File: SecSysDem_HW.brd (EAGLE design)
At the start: 99 x 80 mm, 47 parts, among them Q1 2N3904, T1 MOSFET_NCHANNEL_ENHANCEMENT2N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, T2 MOSFET_NCHANNEL_ENHANCEMENT2N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, T3 MOSFET_NCHANNEL_ENHANCEMENT2N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, U1 XPLAINED_MINI_PINOUT, U2 PCF8574_IO_EXPANDER, U4 FT24C512A, U5 MCP4901-E/SN, X1 C-GRID-06-70553, X5 C-GRID-02-70543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

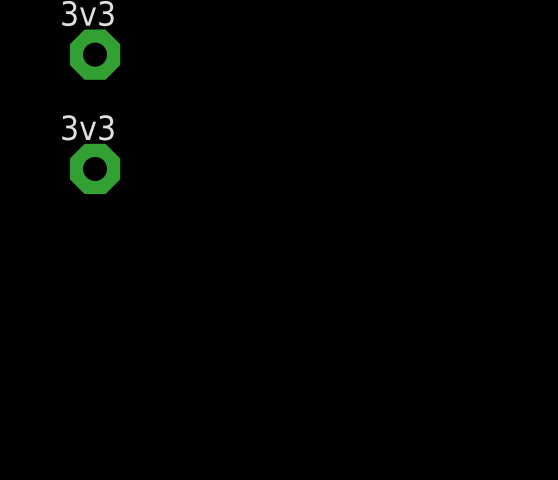
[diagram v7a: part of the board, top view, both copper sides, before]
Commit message: Switched IO expander pins to be keypad pins.
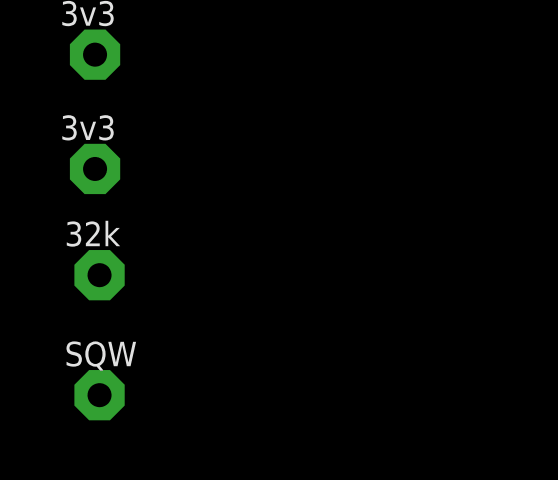
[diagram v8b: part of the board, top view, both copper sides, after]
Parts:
- added V10: SQW, Luke:VIA1
- added V2: 32k, Luke:VIA1
- IC1: value (none) -> L7805 5V
- JP2, JP3, JP4, JP5, JP6: value (none) -> F
- JP7: value (none) -> M
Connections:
- new net N$12: V2.P$1, X1.6
- new net N$20: V10.P$1, X1.5
- net BELL_RINGER: now also U1.P$21; no longer U2.12
- net DOORLOCK_SOLENOID: now also U1.P$20; no longer U2.11
- net KEYPAD_1: now also U2.5; no longer U1.P$6
- net KEYPAD_2: now also U2.6; no longer U1.P$5
- net KEYPAD_3: now also U2.7; no longer U1.P$4
- net KEYPAD_4: now also U2.9; no longer U1.P$17
- net KEYPAD_5: now also U2.10; no longer U1.P$18
- net KEYPAD_6: now also U2.11; no longer U1.P$19
- net KEYPAD_7: now also U2.12; no longer U1.P$20
- net LCD_BACKLIGHT: now also U1.P$22; no longer U1.P$21
- net LCD_DC: now also U1.P$17; no longer U2.7
- net LCD_RST: now also U1.P$18; no longer U2.9
- net LCD_SS: now also U1.P$19; no longer U2.10
- net PUSH_BUTTON: now also U2.4; no longer U1.P$22
- net RGB_BLU: now also U1.P$4; no longer U2.6
- net RGB_GRN: now also U1.P$5; no longer U2.5
- net RGB_RED: now also U1.P$6; no longer U2.4
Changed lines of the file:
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@@
 <attribute name="PROD_ID" value="PRT-10811" x="17.75" y="70" size="1.778" layer="28" rot="MR180" display="off"/>
 </element>
-<element name="IC1" library="v-reg" package="78XXL" value="" x="17.24" y="42.96" rot="MR270"/>
+<element name="IC1" library="v-reg" package="78XXL" value="L7805 5V" x="17.24" y="42.96" rot="MR270"/>
 <element name="C2" library="Luke" package="C0805" value="1uF" x="15.22" y="47.13" rot="R180"/>
 <element name="C3" library="Luke" package="C0805" value="1uF" x="15.22" y="39.94" rot="R180"/>
@@
 <element name="R11" library="Luke" package="C0805" value="100" x="71.84" y="3.88" rot="R270"/>
 <element name="D1" library="diode" package="DO41-7.6" value="1N5819-T" x="12.24" y="24.34" rot="MR270"/>
-<element name="JP2" library="SparkFun-Connectors" package="1X03" value="" x="28" y="65" rot="MR180"/>
-<element name="JP3" library="SparkFun-Connectors" package="1X03" value="" x="28" y="60" rot="MR180"/>
-<element name="JP4" library="SparkFun-Connectors" package="1X03" value="" x="84" y="-7" rot="MR180"/>
-<element name="JP5" library="SparkFun-Connectors" package="1X02" value="" x="17" y="15" rot="R180"/>
-<element name="JP6" library="SparkFun-Connectors" package="1X04" value="" x="67" y="8" rot="R270"/>
-<element name="JP7" library="SparkFun-Connectors" package="1X07" value="" x="41" y="0" rot="R180"/>
+<element name="JP2" library="SparkFun-Connectors" package="1X03" value="F" x="28" y="65" rot="MR180"/>
+<element name="JP3" library="SparkFun-Connectors" package="1X03" value="F" x="28" y="60" rot="MR180"/>
+<element name="JP4" library="SparkFun-Connectors" package="1X03" value="F" x="84" y="-7" rot="MR180"/>
+<element name="JP5" library="SparkFun-Connectors" package="1X02" value="F" x="17" y="15" rot="R180"/>
+<element name="JP6" library="SparkFun-Connectors" package="1X04" value="F" x="67" y="8" rot="R270"/>
+<element name="JP7" library="SparkFun-Connectors" package="1X07" value="M" x="41" y="0" rot="R180"/>
 <element name="U5" library="Luke" package="8-SOIC" value="MCP4901-E/SN" x="47" y="57" rot="R90"/>
+<element name="V2" library="Luke" package="VIA1" value="32k" x="-49" y="-95"/>
+<element name="V10" library="Luke" package="VIA1" value="SQW" x="-49" y="-99"/>
 </elements>
 <signals>
@@
 </signal>
 <signal name="KEYPAD_4">
-<contactref element="U1" pad="P$17"/>
 <contactref element="JP7" pad="4"/>
-<wire x1="33.38" y1="0" x2="49.34" y2="63.92" width="0" layer="19" extent="1-1"/>
+<contactref element="U2" pad="9"/>
+<wire x1="33.38" y1="0" x2="23.08" y2="23.53" width="0" layer="19" extent="1-1"/>
 </signal>
 <signal name="KEYPAD_5">
-<contactref element="U1" pad="P$18"/>
 <contactref element="JP7" pad="5"/>
-<wire x1="30.84" y1="0" x2="51.88" y2="63.92" width="0" layer="19" extent="1-1"/>
+<contactref element="U2" pad="10"/>
+<wire x1="30.84" y1="0" x2="23.08" y2="20.99" width="0" layer="19" extent="1-1"/>
 </signal>
 <signal name="KEYPAD_6">
-<contactref element="U1" pad="P$19"/>
 <contactref element="JP7" pad="6"/>
-<wire x1="28.3" y1="0" x2="54.42" y2="63.92" width="0" layer="19" extent="1-1"/>
+<contactref element="U2" pad="11"/>
+<wire x1="28.3" y1="0" x2="23.08" y2="18.45" width="0" layer="19" extent="1-1"/>
 </signal>
 <signal name="KEYPAD_7">
-<contactref element="U1" pad="P$20"/>
 <contactref element="JP7" pad="7"/>
-<wire x1="25.76" y1="0" x2="56.96" y2="63.92" width="0" layer="19" extent="1-1"/>
+<contactref element="U2" pad="12"/>
+<wire x1="25.76" y1="0" x2="23.08" y2="15.91" width="0" layer="19" extent="1-1"/>
 </signal>
 <signal name="LCD_BACKLIGHT">
-<contactref element="U1" pad="P$21"/>
 <contactref element="R10" pad="1"/>
-<wire x1="59.65" y1="59.83" x2="59.5" y2="63.92" width="0" layer="19" extent="1-1"/>
+<contactref element="U1" pad="P$22"/>
+<wire x1="59.65" y1="59.83" x2="62.04" y2="63.92" width="0" layer="19" extent="1-1"/>
 </signal>
 <signal name="PUSH_BUTTON">
-<contactref element="U1" pad="P$22"/>
 <contactref element="S2" pad="3" route="any" routetag="G$1.2"/>
 <contactref element="S2" pad="4" route="any" routetag="G$1.2"/>
 <contactref element="C4" pad="1"/>
-<wire x1="82.95" y1="10" x2="62.04" y2="63.92" width="0" layer="19" extent="1-1"/>
+<contactref element="U2" pad="4"/>
 <wire x1="85.2606" y1="7.2512" x2="82.95" y2="10" width="0" layer="19" extent="1-1"/>
+<wire x1="30.7" y1="13.37" x2="82.95" y2="10" width="0" layer="19" extent="1-1"/>
 </signal>
 <signal name="KEYPAD_1">
-<contactref element="U1" pad="P$6"/>
 <contactref element="JP7" pad="1"/>
-<wire x1="41" y1="0" x2="56.96" y2="15.66" width="0" layer="19" extent="1-1"/>
+<contactref element="U2" pad="5"/>
+<wire x1="41" y1="0" x2="30.7" y2="15.91" width="0" layer="19" extent="1-1"/>
 </signal>
 <signal name="KEYPAD_2">
-<contactref element="U1" pad="P$5"/>
 <contactref element="JP7" pad="2"/>
-<wire x1="38.46" y1="0" x2="54.42" y2="15.66" width="0" layer="19" extent="1-1"/>
+<contactref element="U2" pad="6"/>
+<wire x1="38.46" y1="0" x2="30.7" y2="18.45" width="0" layer="19" extent="1-1"/>
 </signal>
 <signal name="KEYPAD_3">
-<contactref element="U1" pad="P$4"/>
 <contactref element="JP7" pad="3"/>
-<wire x1="35.92" y1="0" x2="51.88" y2="15.66" width="0" layer="19" extent="1-1"/>
+<contactref element="U2" pad="7"/>
+<wire x1="35.92" y1="0" x2="30.7" y2="20.99" width="0" layer="19" extent="1-1"/>
 </signal>
 <signal name="PIR_SENSOR">
@@
 </signal>
 <signal name="RGB_RED">
-<contactref element="U2" pad="4"/>
 <contactref element="R1" pad="1"/>
-<wire x1="30.7" y1="13.37" x2="62.05" y2="0" width="0" layer="19" extent="1-1"/>
+<contactref element="U1" pad="P$6"/>
+<wire x1="62.05" y1="0" x2="56.96" y2="15.66" width="0" layer="19" extent="1-1"/>
 </signal>
 <signal name="RGB_GRN">
-<contactref element="U2" pad="5"/>
 <contactref element="R2" pad="1"/>
-<wire x1="30.7" y1="15.91" x2="62.06" y2="5.02" width="0" layer="19" extent="1-1"/>
+<contactref element="U1" pad="P$5"/>
+<wire x1="62.06" y1="5.02" x2="54.42" y2="15.66" width="0" layer="19" extent="1-1"/>
 </signal>
 <signal name="RGB_BLU">
-<contactref element="U2" pad="6"/>
 <contactref element="R3" pad="1"/>
-<wire x1="30.7" y1="18.45" x2="62.06" y2="8.21" width="0" layer="19" extent="1-1"/>
+<contactref element="U1" pad="P$4"/>
+<wire x1="51.88" y1="15.66" x2="62.06" y2="8.21" width="0" layer="19" extent="1-1"/>
 </signal>
 <signal name="LCD_DC">
-<contactref element="U2" pad="7"/>
 <contactref element="U$3" pad="P$11" route="any" routetag="G$1.DC"/>
 <contactref element="U$3" pad="P$3" route="any" routetag="G$1.DC"/>
-<wire x1="30.7" y1="20.99" x2="73.19" y2="20" width="0" layer="19" extent="1-1"/>
+<contactref element="U1" pad="P$17"/>
+<wire x1="73.19" y1="59" x2="49.34" y2="63.92" width="0" layer="19" extent="1-1"/>
 </signal>
 <signal name="LCD_RST">
-<contactref element="U2" pad="9"/>
 <contactref element="U$3" pad="P$9" route="any" routetag="G$1.RST"/>
 <contactref element="U$3" pad="P$1" route="any" routetag="G$1.RST"/>
-<wire x1="23.08" y1="23.53" x2="68.11" y2="20" width="0" layer="19" extent="1-1"/>
+<contactref element="U1" pad="P$18"/>
+<wire x1="68.11" y1="59" x2="51.88" y2="63.92" width="0" layer="19" extent="1-1"/>
 </signal>
 <signal name="LCD_SS">
-<contactref element="U2" pad="10"/>
 <contactref element="U$3" pad="P$2" route="any" routetag="G$1.CE"/>
 <contactref element="U$3" pad="P$10" route="any" routetag="G$1.CE"/>
-<wire x1="23.08" y1="20.99" x2="70.65" y2="20" width="0" layer="19" extent="1-1"/>
+<contactref element="U1" pad="P$19"/>
+<wire x1="70.65" y1="59" x2="54.42" y2="63.92" width="0" layer="19" extent="1-1"/>
 </signal>
 <signal name="DOORLOCK_SOLENOID">
-<contactref element="U2" pad="11"/>
 <contactref element="T1" pad="1"/>
-<wire x1="18" y1="20.05" x2="23.08" y2="18.45" width="0" layer="19" extent="1-1"/>
+<contactref element="U1" pad="P$20"/>
+<wire x1="18" y1="20.05" x2="56.96" y2="63.92" width="0" layer="19" extent="1-1"/>
 </signal>
 <signal name="BELL_RINGER">
-<contactref element="U2" pad="12"/>
 <contactref element="T3" pad="1"/>
-<wire x1="14.56" y1="3.63" x2="23.08" y2="15.91" width="0" layer="19" extent="1-1"/>
+<contactref element="U1" pad="P$21"/>
+<wire x1="14.56" y1="3.63" x2="59.5" y2="63.92" width="0" layer="19" extent="1-1"/>
 </signal>
 <signal name="N$2">
@@
 <wire x1="49.6" y1="56.365" x2="71.184" y2="63.92" width="0" layer="19" extent="1-1"/>
 </signal>
+<signal name="N$12">
+<contactref element="X1" pad="6"/>
+<contactref element="V2" pad="P$1"/>
+<wire x1="27.1" y1="44.81" x2="-49" y2="-95" width="0" layer="19" extent="1-1"/>
+</signal>
+<signal name="N$20">
+<contactref element="X1" pad="5"/>
+<contactref element="V10" pad="P$1"/>
+<wire x1="27.1" y1="42.27" x2="-49" y2="-99" width="0" layer="19" extent="1-1"/>
+</signal>
 </signals>
